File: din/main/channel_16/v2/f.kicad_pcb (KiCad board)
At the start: 2 copper layers, 76.8 x 81.3 mm, 29 parts, among them J1 fm16_i, J10 wrs_i, J11 selector4_i, J12 Bus88_2x14, J13 dio_channel_i, J14 dio_channel_i, J15 dio_channel_i, J16 dio_channel_i, J17 dio_channel_i, J18 dio_channel_i, J19 dio_channel_i, J2 dio_channel_i, J20 dio_channel_i, J21 wrs_i, J3 dio_channel_i, J4 dio_channel_i, J5 dio_channel_i, J6 dio_channel_i, J7 dio_channel_i, J8 dio_channel_i, J9 dio_channel_i, U1 74LS245, U2 74LS245

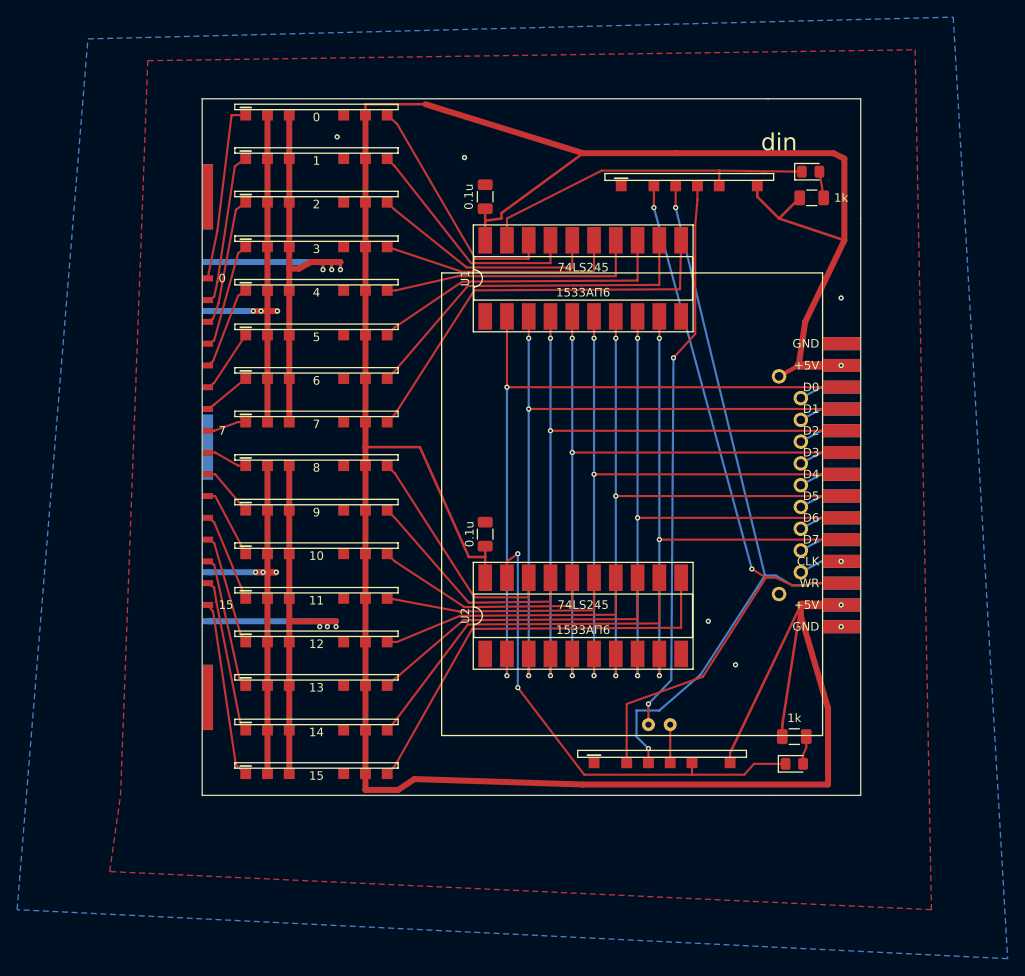
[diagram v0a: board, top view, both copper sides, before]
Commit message: voltage regulator for each module
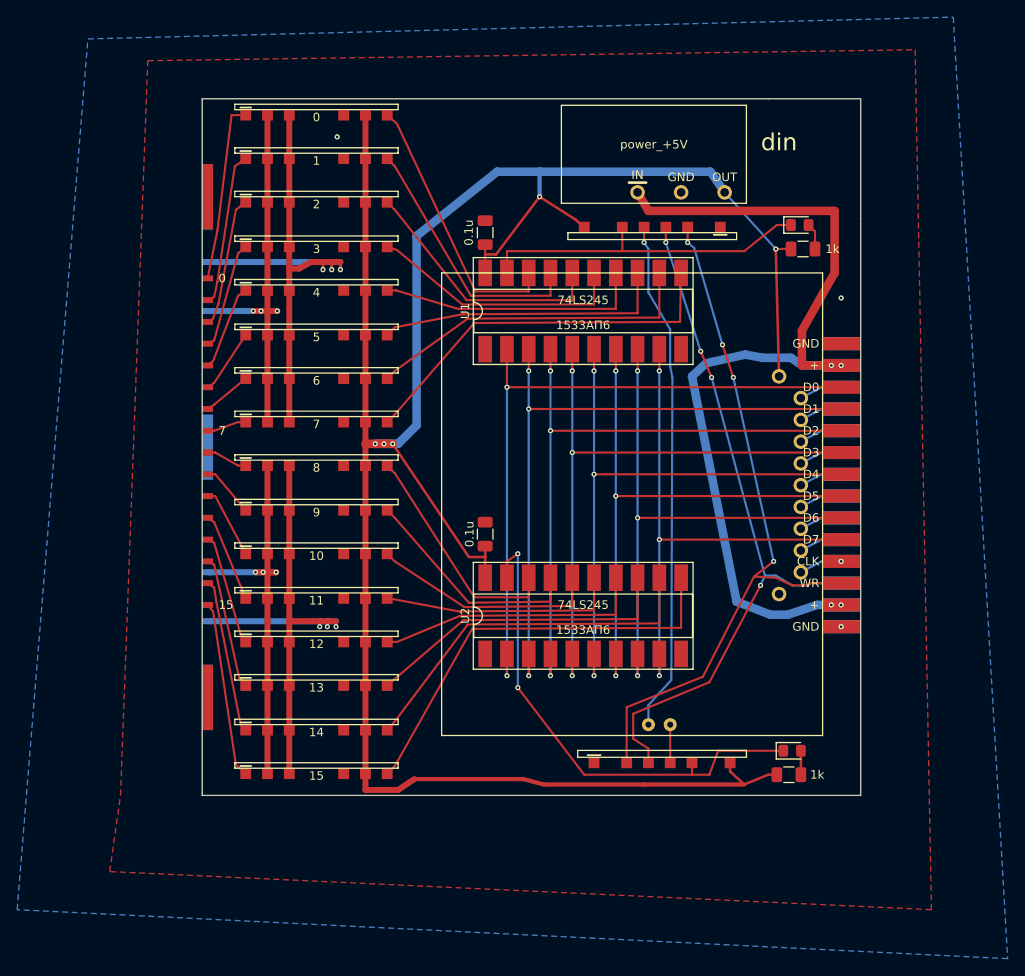
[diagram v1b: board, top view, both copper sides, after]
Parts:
- added J22: bus_i, plc88:bus_im, F.Cu at (108.8, 59.1)
- J12: value Bus88_2x14 -> power_+5V; footprint 1my_elements:Bus88_2x14 -> plc88:power_i
- moved J12 41.0 mm to (78.7, 31.2)
- moved J10 10.2 mm to (87.8, 48.0), turned to 180 degrees
- moved D1 6.35 mm to (104.0, 45.2)
- moved R1 6.05 mm to (104.4, 48.0)
- moved R2 4.49 mm to (102.7, 109.3)
- moved C1 4.19 mm to (67.3, 46.1)
- moved U1 3.81 mm to (78.7, 55.2)
- moved D2 1.55 mm to (103.1, 106.6)
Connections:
- J12 pad 1: GND -> VPBUS
- J12 pad 2: GND -> +5V
- J12 pad 3: +5V -> GND
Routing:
- net VPBUS: track 0.00 -> 105.7 mm, vias 0 -> 4
- net +5V: track 346.3 -> 270.8 mm, vias 2 -> 5
- net S0: track 64.9 -> 59.9 mm, vias 2 -> 1
- net WR: track 87.2 -> 83.0 mm, vias 2 -> 4
- net D7: track 65.7 -> 61.8 mm
- net D6: track 68.2 -> 64.4 mm
- net D3: track 75.8 -> 72.0 mm
- net D2: track 78.4 -> 74.5 mm
- net D0: track 83.4 -> 79.6 mm
- net D5: track 70.7 -> 66.9 mm
- net D4: track 73.3 -> 69.5 mm
- net D1: track 80.9 -> 77.1 mm
- net RD: track 85.5 -> 82.0 mm, vias 2 -> 4
- net INL0: track 28.1 -> 31.5 mm
- net INL1: track 27.5 -> 30.7 mm
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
